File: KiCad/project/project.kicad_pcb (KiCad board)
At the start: 4 copper layers, 50 x 50 mm, 31 parts, among them P1 TerminalBlock 5P 5.0mm, U1 DRV8313PWPR

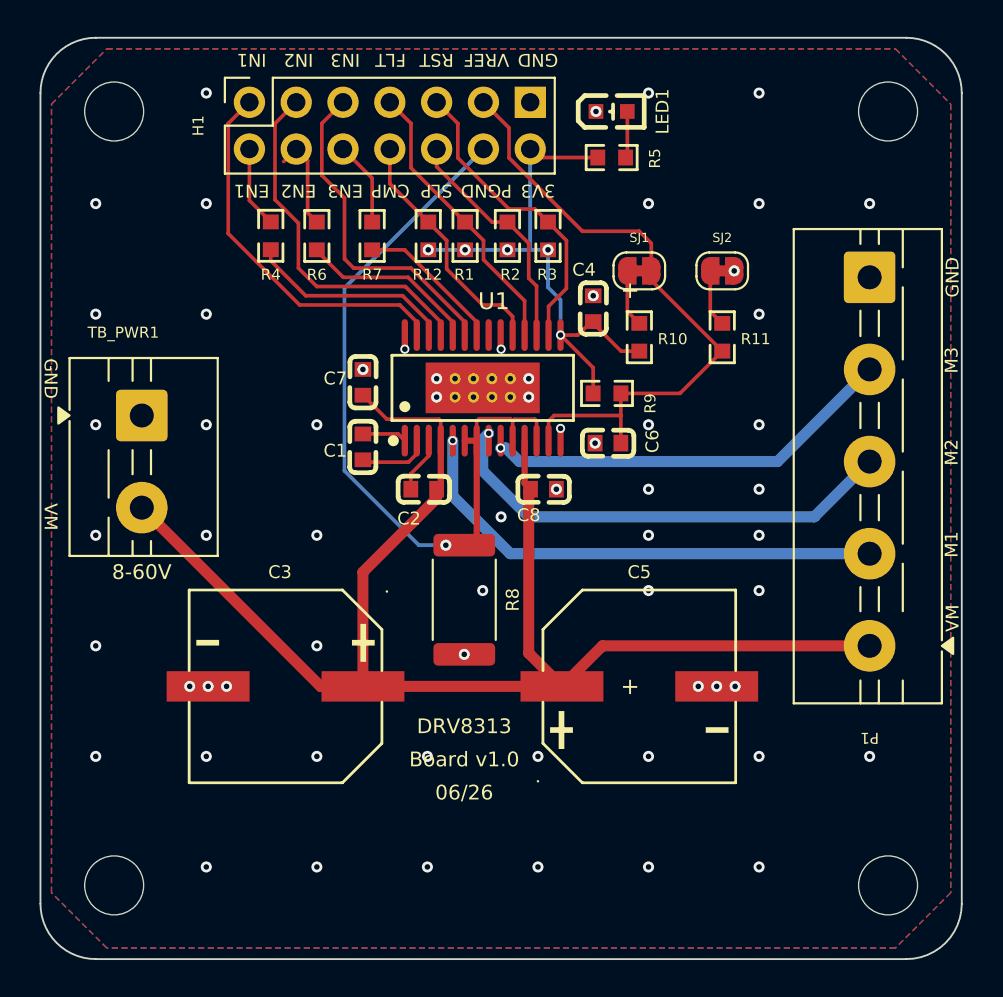
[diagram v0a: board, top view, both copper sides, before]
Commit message: Rework
Remove resistors on enable lines.
Redo board layout with clearer and wider power paths.
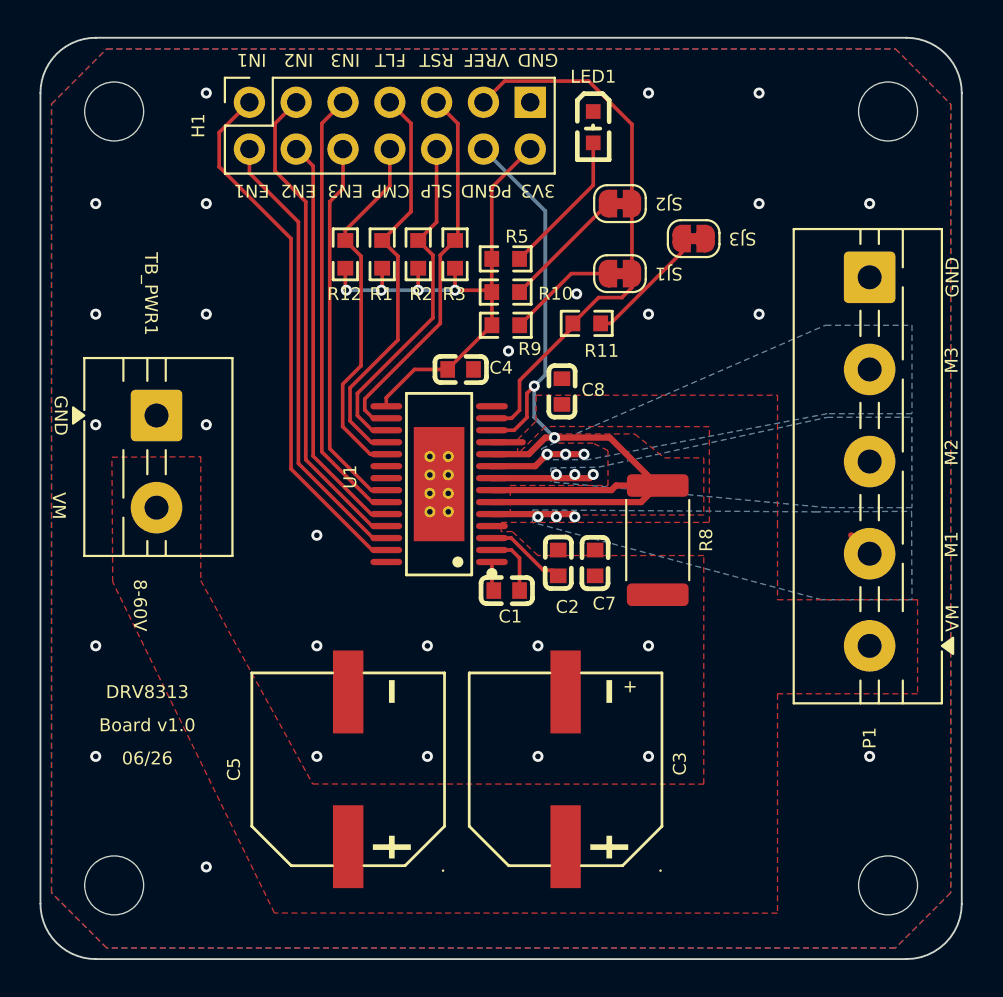
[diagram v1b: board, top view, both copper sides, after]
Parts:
- removed C6: 470nF, drv8313-board:C0603
- removed R4, R6, R7: 10kΩ, drv8313-board:R0603
- added SJ3: JMP, Jumper:SolderJumper-2_P1.3mm_Bridged_RoundedPad1.0x1.5mm, F.Cu at (169.4, 98.9)
- C2: value 100nF -> 100nF 16V
- moved C5 16.4 mm to (150.7, 127.7), turned to 90 degrees
- moved C7 16.0 mm to (164.1, 116.5), turned to 90 degrees
- moved C3 15.9 mm to (162.5, 127.7), turned to 90 degrees
- moved C1 11.0 mm to (159.3, 118.0), turned to 180 degrees
- moved R8 11.0 mm to (167.5, 115.3)
- moved C2 8.32 mm to (162.1, 116.5), turned to -90 degrees
- moved R5 7.96 mm to (159.2, 100.0)
- moved C4 7.92 mm to (156.8, 106.0), turned to 180 degrees
- moved R10 7.66 mm to (159.2, 101.8), turned to 0 degrees
- moved R11 7.39 mm to (163.6, 103.5), turned to 0 degrees
- moved SJ2 6.64 mm to (165.4, 97.0)
- moved R9 6.62 mm to (159.3, 103.6)
- moved U1 5.74 mm to (155.6, 112.2), turned to 90 degrees
- moved C8 5.39 mm to (162.3, 107.2), turned to -90 degrees
- moved R3 5.14 mm to (156.5, 99.8)
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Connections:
- H1 pad 2: EN1H -> EN1
- H1 pad 4: EN2H -> EN2
- H1 pad 6: EN3H -> EN3
- R10 pad 2: XN -> Net-(SJ2-A)
- R11 pad 2: YN -> Net-(SJ3-A)
- R9 pad 2: VREF -> Net-(SJ1-A)
- SJ1 pad 1: XN -> Net-(SJ1-A)
- SJ2 pad 1: YN -> Net-(SJ2-A)
- SJ2 pad 2: GND -> VREF
- U1 pad 21: unconnected-(U1-NC-Pad21) -> GND
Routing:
- net VCC: track 79.7 -> 1.68 mm
- net M1: track 27.7 -> 5.98 mm, vias 1 -> 3
- net M2: track 25.4 -> 6.86 mm, vias 1 -> 3
- net M3: track 22.6 -> 5.27 mm, vias 1 -> 3
- net EN1: track 11.3 -> 24.6 mm
- net EN2: track 9.70 -> 22.3 mm
- net EN3: track 8.04 -> 20.6 mm
- net PGND: track 41.1 -> 50.9 mm, vias 1 -> 2
- net IN1: track 20.6 -> 29.7 mm
- net IN2: track 19.7 -> 27.2 mm
- net Net-(SJ2-A): track 0.00 -> 6.79 mm
- net Net-(SJ3-A): track 0.00 -> 6.75 mm
- net nFlt: track 15.7 -> 22.3 mm
- net nCOMPO: track 13.5 -> 19.8 mm
- net Net-(SJ1-A): track 0.00 -> 5.95 mm
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- added copper zone on B.Cu, net M1
- added copper zone on B.Cu, net M2
- added copper zone on B.Cu, net M3
- added copper zone on F.Cu, net PGND
- added copper zone on F.Cu, net VCC
